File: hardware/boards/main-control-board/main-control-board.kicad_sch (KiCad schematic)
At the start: 8 parts, among them J2 Conn_OLED, J3 Conn_extension, J4 Conn_extension_2

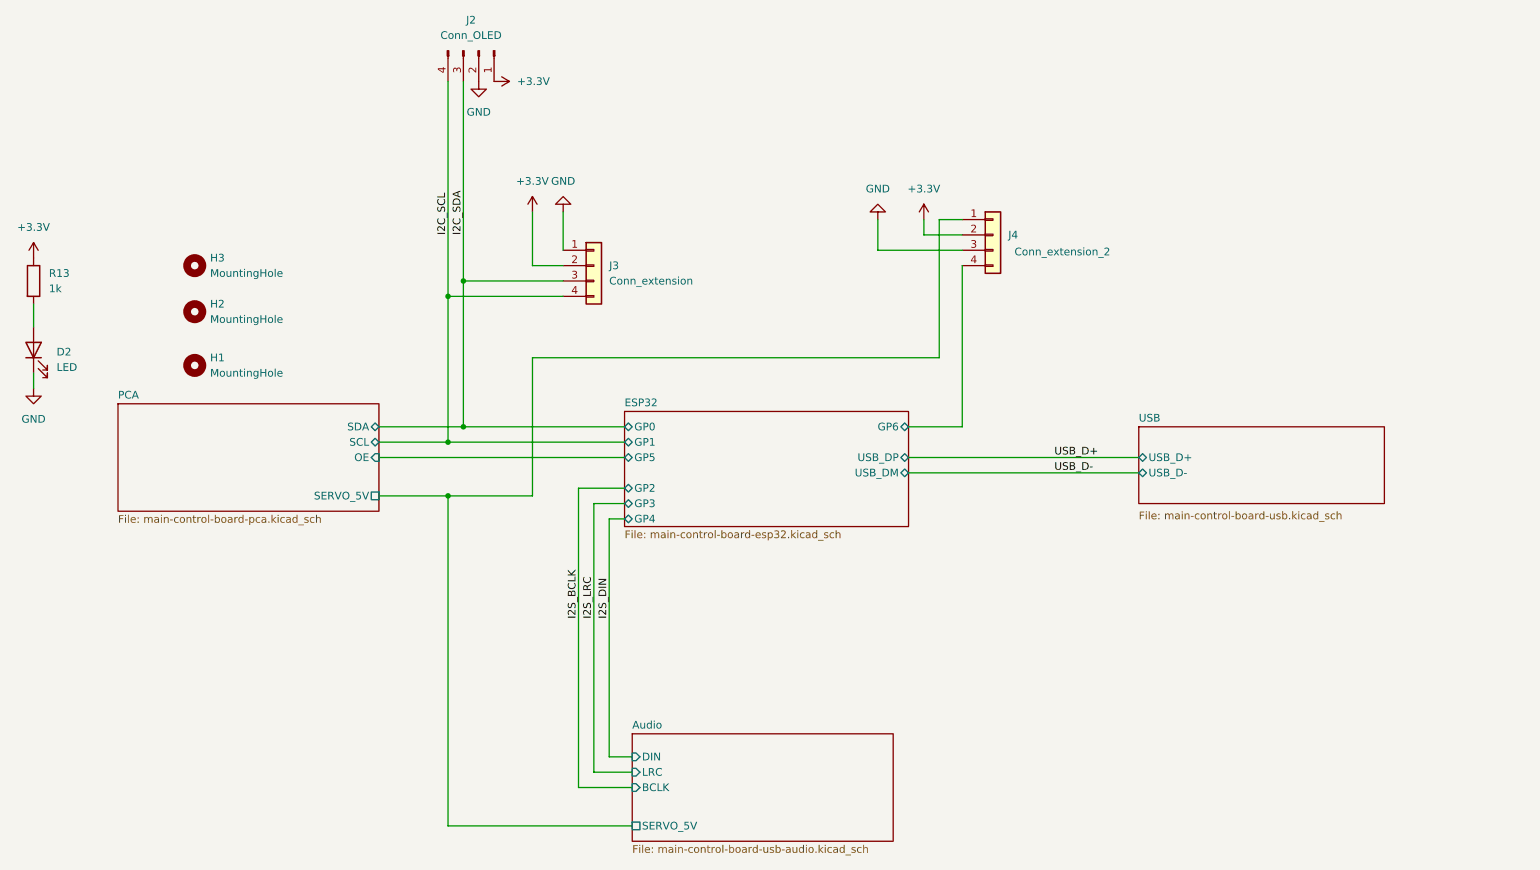
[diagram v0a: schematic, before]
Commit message: add extension port
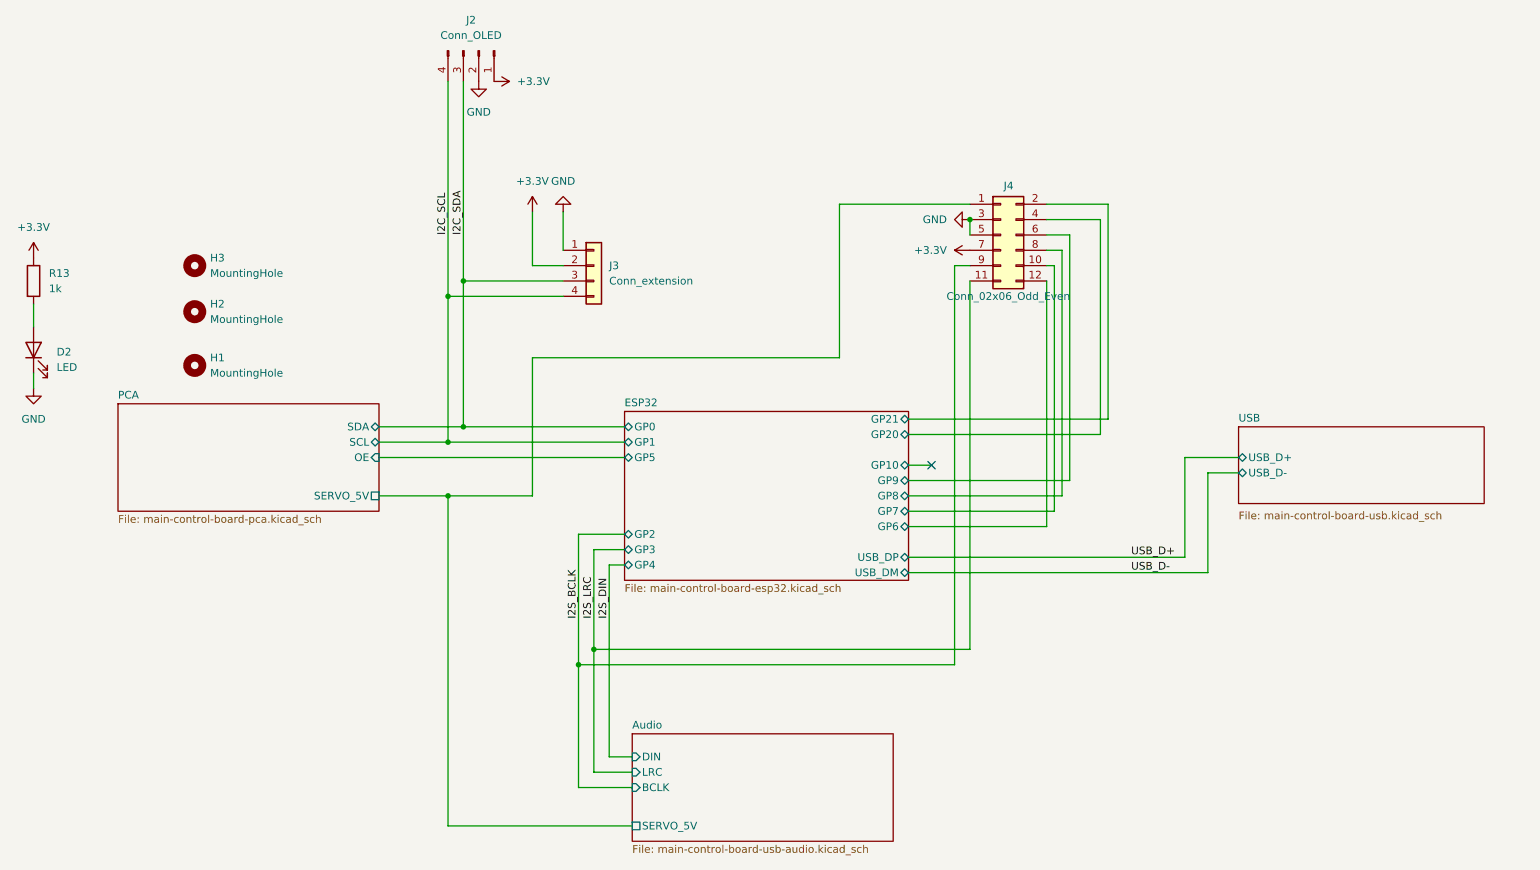
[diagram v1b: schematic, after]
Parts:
- J4: value Conn_extension_2 -> Conn_02x06_Odd_Even; footprint Connector_PinHeader_2.54mm:PinHeader_1x04_P2.54mm_Vertical -> Connector_PinHeader_2.54mm:PinHeader_2x06_P2.54mm_Vertical; symbol Connector_Generic:Conn_01x04 -> Connector_Generic:Conn_02x06_Odd_Even; now in the parts list
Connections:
- net +3.3V: now also J4.7 (Pin_7); no longer J4.2 (Pin_2)
- net ESP32/GP6: now also J4.12 (Pin_12); no longer J4.4 (Pin_4)
- net GND: now also J4.5 (Pin_5)
- net I2S_BCLK: now also J4.9 (Pin_9)
- net I2S_LRC: now also J4.11 (Pin_11)
- new net ESP32/GP20: J4.4 (Pin_4)
- new net ESP32/GP21: J4.2 (Pin_2)
- new net ESP32/GP7: J4.10 (Pin_10)
- new net ESP32/GP8: J4.8 (Pin_8)
- new net ESP32/GP9: J4.6 (Pin_6)
- no-connect marks 0 -> 1
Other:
- sheet ESP32 ports: added GP10, GP20, GP21, GP7, GP8, GP9; removed none

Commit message: update BOM
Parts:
- J4: FT Rotation Offset (none) -> 90; LCSC Part # (none) -> C541855; MPN (none) -> PM254V-12-12-H85; Manufacturer (none) -> XFCN
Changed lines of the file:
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@@
 	(title_block
 		(title "TinyEngineer PCB")
-		(date "2026-09-24")
-		(rev "v2")
+		(date "2026-10-06")
+		(rev "v3")
 	)
 	(junction
@@
 	(wire
 		(pts
-			(xy 209.55 104.14) (xy 209.55 63.5)
-		)
-		(stroke
-			(width 0)
-			(type default)
-		)
-	)
-	(wire
-		(pts
-			(xy 186.69 96.52) (xy 213.36 96.52)
+			(xy 212.09 104.14) (xy 212.09 63.5)
+		)
+		(stroke
+			(width 0)
+			(type default)
+		)
+	)
+	(wire
+		(pts
+			(xy 186.69 96.52) (xy 219.71 96.52)
 		)
 		(stroke
@@
 	(wire
 		(pts
-			(xy 218.44 88.9) (xy 218.44 53.34)
-		)
-		(stroke
-			(width 0)
-			(type default)
-		)
-	)
-	(wire
-		(pts
-			(xy 213.36 55.88) (xy 209.55 55.88)
+			(xy 224.79 88.9) (xy 224.79 53.34)
+		)
+		(stroke
+			(width 0)
+			(type default)
+		)
+	)
+	(wire
+		(pts
+			(xy 219.71 55.88) (xy 209.55 55.88)
 		)
 		(stroke
@@
 	(wire
 		(pts
-			(xy 210.82 101.6) (xy 210.82 60.96)
-		)
-		(stroke
-			(width 0)
-			(type default)
-		)
-	)
-	(wire
-		(pts
-			(xy 186.69 104.14) (xy 209.55 104.14)
+			(xy 214.63 101.6) (xy 214.63 60.96)
+		)
+		(stroke
+			(width 0)
+			(type default)
+		)
+	)
+	(wire
+		(pts
+			(xy 186.69 104.14) (xy 212.09 104.14)
 		)
 		(stroke
@@
 	(wire
 		(pts
-			(xy 186.69 101.6) (xy 210.82 101.6)
-		)
-		(stroke
-			(width 0)
-			(type default)
-		)
-	)
-	(wire
-		(pts
-			(xy 186.69 99.06) (xy 212.09 99.06)
-		)
-		(stroke
-			(width 0)
-			(type default)
-		)
-	)
-	(wire
-		(pts
-			(xy 219.71 86.36) (xy 219.71 50.8)
+			(xy 186.69 101.6) (xy 214.63 101.6)
+		)
+		(stroke
+			(width 0)
+			(type default)
+		)
+	)
+	(wire
+		(pts
+			(xy 186.69 99.06) (xy 217.17 99.06)
+		)
+		(stroke
+			(width 0)
+			(type default)
+		)
+	)
+	(wire
+		(pts
+			(xy 226.06 86.36) (xy 226.06 50.8)
 		)
 		(stroke
@@
 	(wire
 		(pts
-			(xy 213.36 96.52) (xy 213.36 55.88)
+			(xy 219.71 96.52) (xy 219.71 55.88)
 		)
 		(stroke
@@
 	(wire
 		(pts
-			(xy 218.44 53.34) (xy 209.55 53.34)
+			(xy 224.79 53.34) (xy 209.55 53.34)
 		)
 		(stroke
@@
 	(wire
 		(pts
-			(xy 210.82 60.96) (xy 209.55 60.96)
+			(xy 214.63 60.96) (xy 209.55 60.96)
 		)
 		(stroke
@@
 	(wire
 		(pts
-			(xy 212.09 58.42) (xy 209.55 58.42)
+			(xy 217.17 58.42) (xy 209.55 58.42)
 		)
 		(stroke
@@
 	(wire
 		(pts
-			(xy 212.09 99.06) (xy 212.09 58.42)
+			(xy 217.17 99.06) (xy 217.17 58.42)
 		)
 		(stroke
@@
 	(wire
 		(pts
+			(xy 212.09 63.5) (xy 209.55 63.5)
+		)
+		(stroke
+			(width 0)
+			(type default)
+		)
+	)
+	(wire
+		(pts
 			(xy 113.03 63.5) (xy 113.03 87.63)
 		)
@@
 	(wire
 		(pts
-			(xy 219.71 50.8) (xy 209.55 50.8)
+			(xy 226.06 50.8) (xy 209.55 50.8)
 		)
 		(stroke
@@
 	(wire
 		(pts
-			(xy 186.69 88.9) (xy 218.44 88.9)
+			(xy 186.69 88.9) (xy 224.79 88.9)
 		)
 		(stroke
@@
 	(wire
 		(pts
-			(xy 186.69 86.36) (xy 219.71 86.36)
+			(xy 186.69 86.36) (xy 226.06 86.36)
 		)
 		(stroke
@@
 			(at 201.93 55.88 0)
 			(hide yes)
+			(show_name no)
+			(do_not_autoplace no)
+			(effects
+				(font
+					(size 1.27 1.27)
+				)
+			)
+		)
+		(property "LCSC Part #" "C541855"
+			(at 201.93 55.88 0)
+			(hide yes)
+			(show_name no)
+			(do_not_autoplace no)
+			(effects
+				(font
+					(size 1.27 1.27)
+				)
+			)
+		)
+		(property "MPN" "PM254V-12-12-H85"
+			(at 201.93 55.88 0)
+			(hide yes)
+			(show_name no)
+			(do_not_autoplace no)
+			(effects
+				(font
+					(size 1.27 1.27)
+				)
+			)
+		)
+		(property "Manufacturer" "XFCN"
+			(at 201.93 55.88 0)
+			(hide yes)
+			(show_name no)
+			(do_not_autoplace no)
+			(effects
+				(font
+					(size 1.27 1.27)
+				)
+			)
+		)
+		(property "FT Rotation Offset" "90"
+			(at 201.93 55.88 0)
+			(hide yes)
